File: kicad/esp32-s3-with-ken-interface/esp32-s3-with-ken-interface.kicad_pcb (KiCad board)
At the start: 4 copper layers, 50.8 x 81.3 mm, 28 parts, among them J1 TYPE-C-31-M-12, Q1 UMH3N, U1 CH340C, U2 AMS1117-3.3, U3 XDZ254-2-15-W-2.5-G1, U4 ESP32-S3-WROOM-1, U5 PM254-2-15-W-8.5

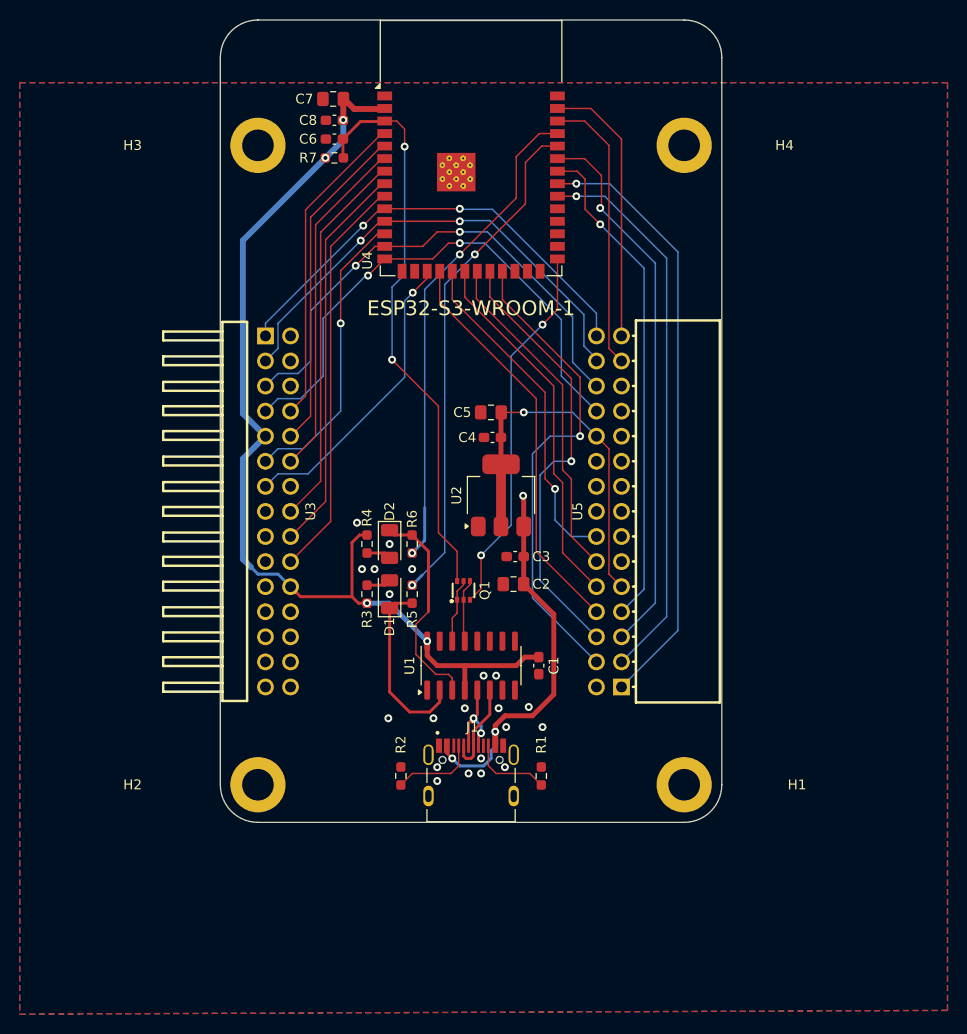
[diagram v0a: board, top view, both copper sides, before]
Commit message: fix left pin header pin assignment
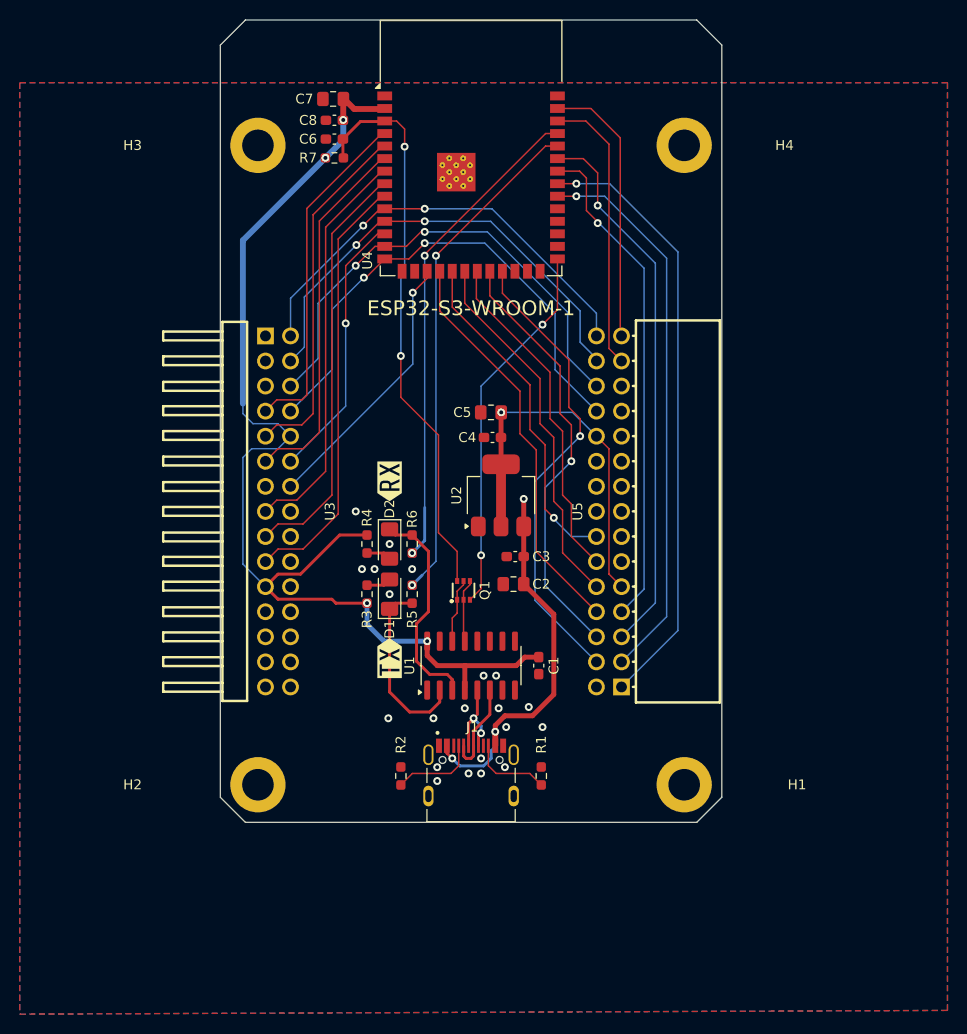
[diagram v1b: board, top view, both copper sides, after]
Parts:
- added kibuzzard-696F5E7C: G***, kibuzzard-696F5E7C, F.Cu at (75.6, 104.0)
- added kibuzzard-696F5E93: G***, kibuzzard-696F5E93, F.Cu at (75.6, 86.1)
- D1, D2: footprint LED_SMD:LED_1206_3216Metric -> LED_SMD:LED_1206_3216Metric_Pad1.42x1.75mm_HandSolder
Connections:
- U3 pad 1: /IO17 -> /ADC_1
- U3 pad 10: /I2S_SCK -> +3V3
- U3 pad 11: /I2C_A_SDA -> /I2S_SD
- U3 pad 12: /I2S_SD -> /I2C_A_SDA
- U3 pad 13: /I2C_A_SCL -> VBUS
- U3 pad 14: VBUS -> /I2C_A_SCL
- U3 pad 15: GND -> /I2S_B_DIN
- U3 pad 16: /I2S_B_DIN -> GND
- U3 pad 17: /IO11 -> /I2S_B_BCLK
- U3 pad 18: /I2S_B_BCLK -> /IO11
- U3 pad 19: /IO13 -> /I2S_B_LRC
- U3 pad 2: /ADC_1 -> /IO17
- U3 pad 20: /I2S_B_LRC -> /IO13
- U3 pad 21: /IO12 -> +3V3
- U3 pad 22: +3V3 -> /IO12
- U3 pad 23: /IO10 -> /I2C_B_SDA
- U3 pad 24: /I2C_B_SDA -> /IO10
- U3 pad 25: /BTN_A -> /I2C_B_SCL
- U3 pad 26: /I2C_B_SCL -> /BTN_A
- U3 pad 27: /BTN_B -> /BTN_C
- U3 pad 28: /BTN_C -> /BTN_B
- U3 pad 29: GND -> /BTN_D
- U3 pad 3: /IO18 -> /ADC_2
- U3 pad 30: /BTN_D -> GND
- U3 pad 4: /ADC_2 -> /IO18
- U3 pad 5: /IO19 -> GND
- U3 pad 6: GND -> /IO19
- U3 pad 7: /IO20 -> /I2S_WS
- U3 pad 8: /I2S_WS -> /IO20
- U3 pad 9: +3V3 -> /I2S_SCK
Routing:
- net +3V3: track 167.6 -> 179.4 mm
- net /I2S_B_BCLK: track 74.9 -> 81.0 mm
- net /I2C_A_SCL: track 64.9 -> 59.6 mm
- net /I2S_B_LRC: track 76.1 -> 81.2 mm
- net /I2S_WS: track 66.8 -> 71.9 mm
- net /I2S_SD: track 69.4 -> 74.4 mm
- net /I2S_SCK: track 68.1 -> 73.2 mm
- net /I2C_A_SDA: track 64.5 -> 59.5 mm
- net /I2S_B_DIN: track 73.2 -> 78.0 mm
- net /BTN_B: track 83.9 -> 79.5 mm
- net /BTN_A: track 79.8 -> 75.6 mm
- net /IO11: track 69.0 -> 65.4 mm
- net /IO10: track 75.6 -> 72.1 mm
- net /IO13: track 69.1 -> 65.5 mm
- net /BTN_C: track 91.0 -> 94.5 mm
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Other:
- outline, holes or cut-outs redrawn

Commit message: adjust traces
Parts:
- moved Q1 0.65 mm to (83.2, 96.5)
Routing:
- net RTS: track 6.57 -> 7.26 mm
- net DTR: track 6.42 -> 7.00 mm
- net RESET: track 57.6 -> 57.0 mm

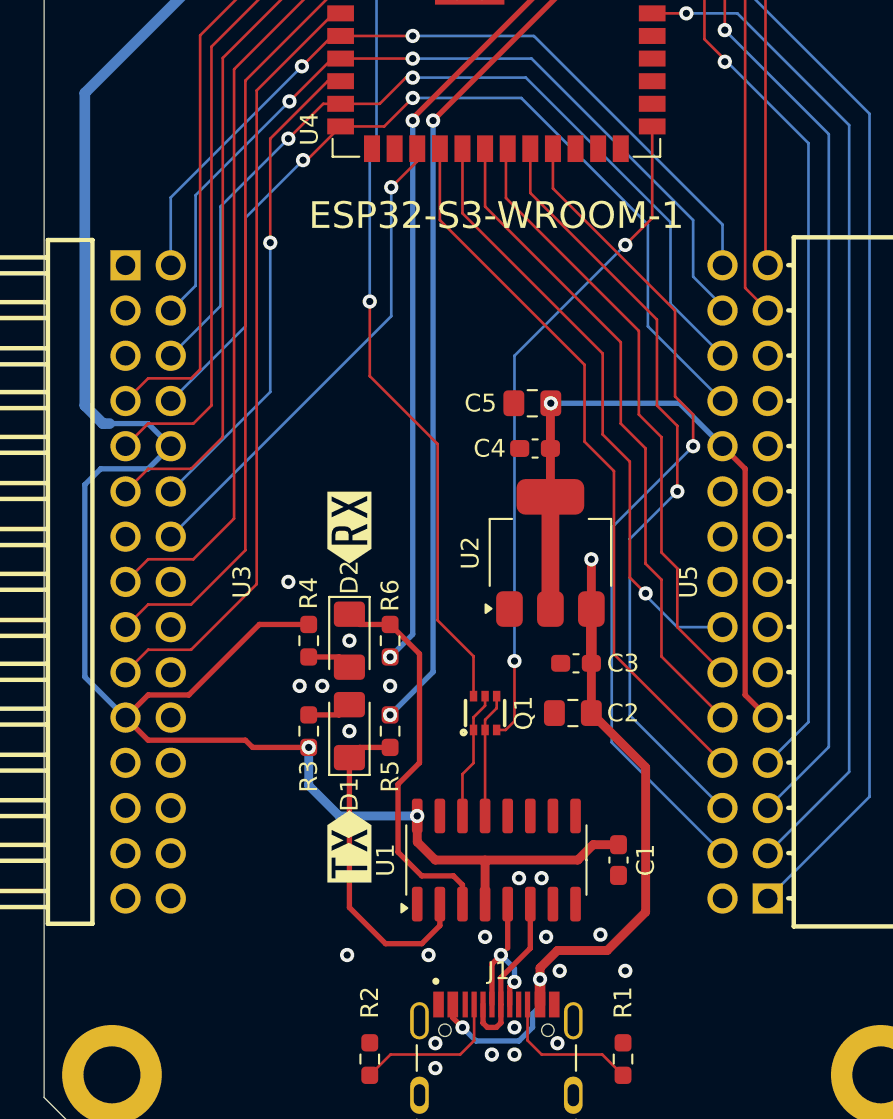
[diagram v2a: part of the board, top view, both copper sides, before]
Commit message: add pin label, adjust routing, add PWM pins
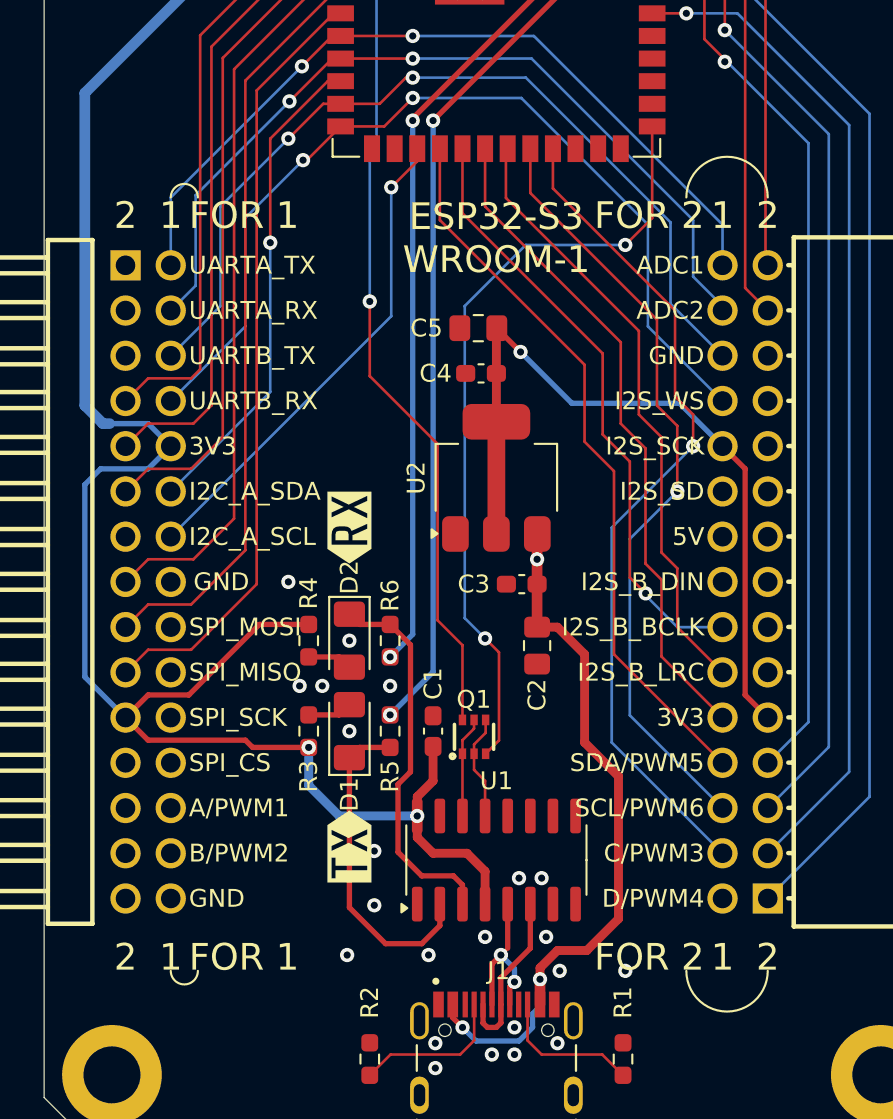
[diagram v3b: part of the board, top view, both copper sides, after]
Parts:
- moved C1 12.7 mm to (80.3, 97.5), turned to 90 degrees
- moved C3 5.39 mm to (85.2, 89.3)
- moved C4 5.19 mm to (83.0, 77.4)
- moved U2 5.19 mm to (83.8, 83.3)
- moved C5 5.19 mm to (82.8, 74.9)
- moved C2 4.29 mm to (86.1, 92.7), turned to -90 degrees
- moved Q1 1.47 mm to (82.6, 97.9)
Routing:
- net GPIO0(D3): track 37.8 -> 44.0 mm
- net VBUS: track 76.6 -> 79.3 mm
- net RTS: track 7.26 -> 5.66 mm
- net RESET: track 57.0 -> 58.1 mm
- net DTR: track 7.00 -> 5.96 mm
- net +3V3: track 179.3 -> 180.0 mm
- net GND: vias 21 -> 22
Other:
- board text added: "1"
- board text added: "2"
- board text added: "3V3"
- board text added: "5V"
- board text added: "A/PWM1"
- board text added: "ADC1"
- board text added: "ADC2"
- board text added: "B/PWM2"
- board text added: "C/PWM3"
- board text added: "D/PWM4"
- board text added: "ESP32-S3 WROOM-1"
- board text added: "FOR 1"
- board text added: "FOR 2"
- board text added: "GND"
- board text added: "I2C_A_SCL"
- board text added: "I2C_A_SDA"
- board text added: "I2S_B_BCLK"
- board text added: "I2S_B_DIN"
- board text added: "I2S_B_LRC"
- board text added: "I2S_SCK"
- board text added: "I2S_SD"
- board text added: "I2S_WS"
- board text added: "SCL/PWM6"
- board text added: "SDA/PWM5"
- board text added: "SPI_CS"
- board text added: "SPI_MISO"
- board text added: "SPI_MOSI"
- board text added: "SPI_SCK"
- board text added: "UARTA_RX"
- board text added: "UARTA_TX"
- board text added: "UARTB_RX"
- board text added: "UARTB_TX"
- board text removed: "ESP32-S3-WROOM-1"

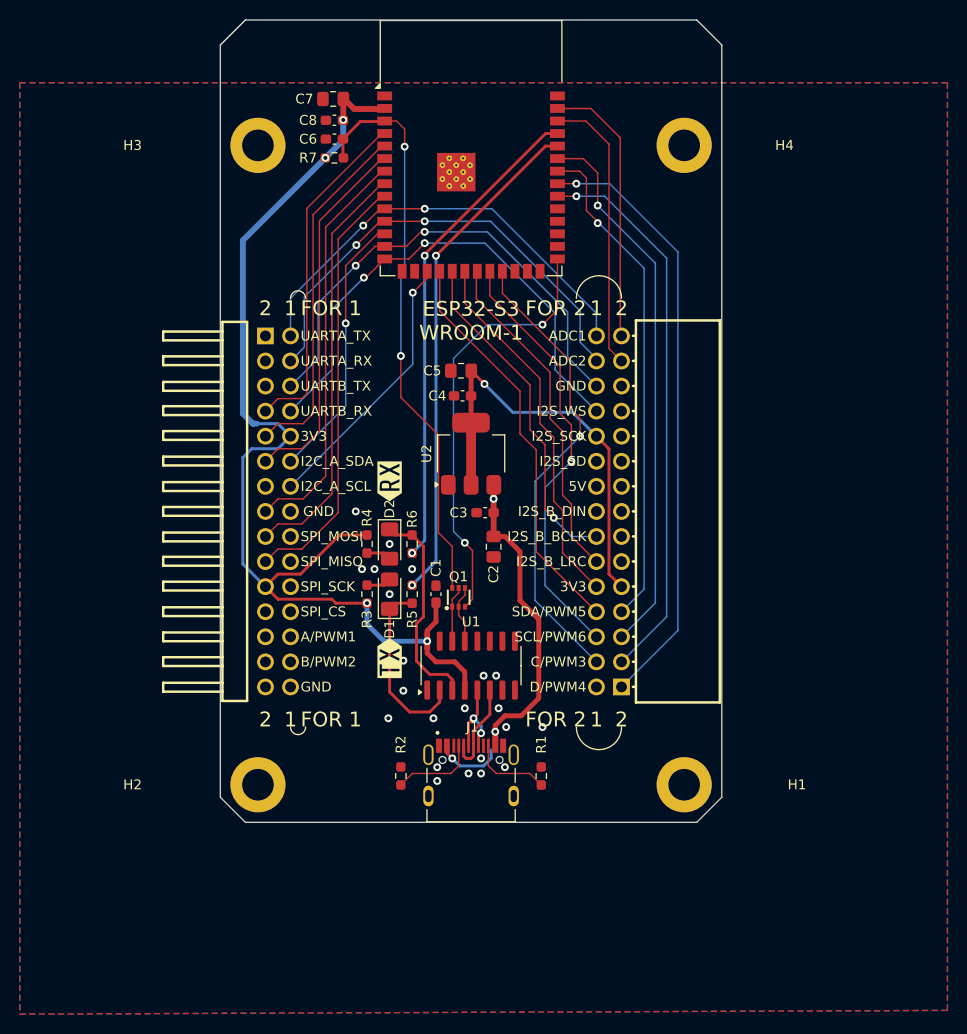
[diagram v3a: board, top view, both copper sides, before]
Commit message: add protect diode, improve trace routing, add vias, add user button and user led, improve schematic, add texts
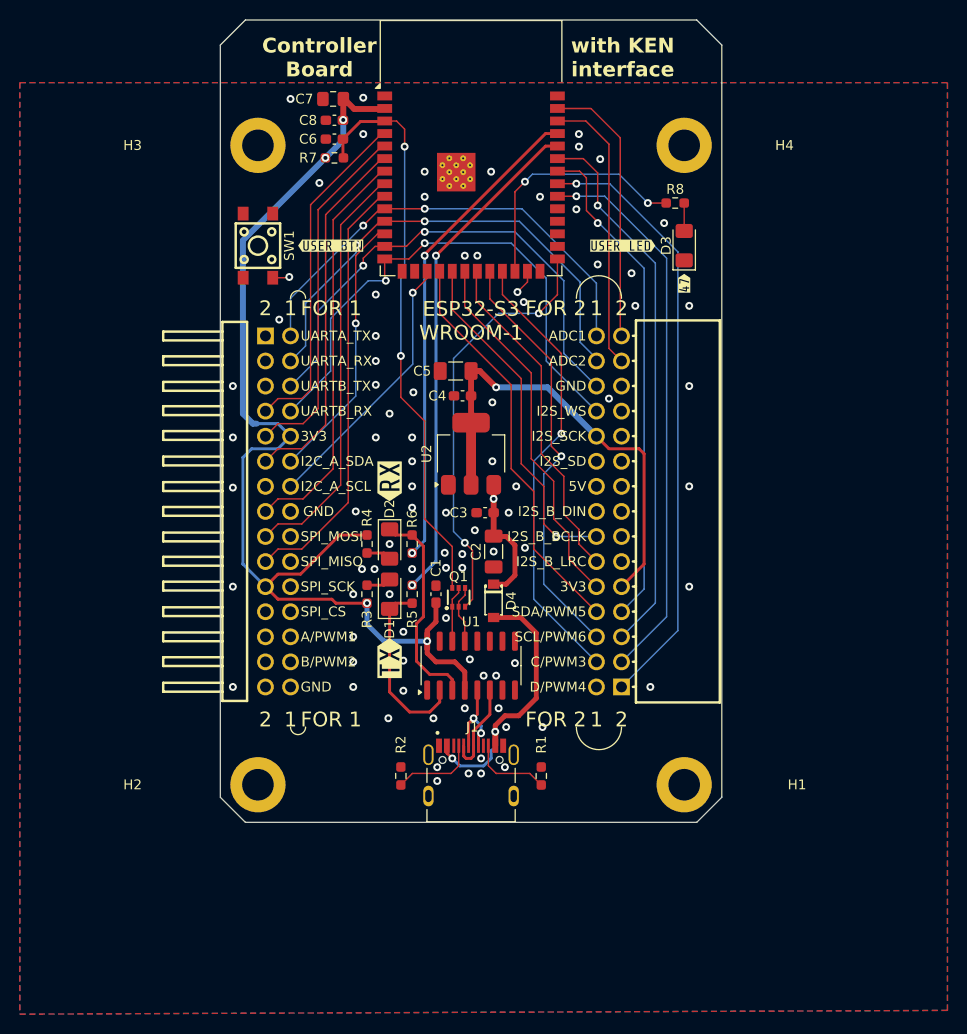
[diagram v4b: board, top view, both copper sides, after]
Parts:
- added D3: LED, LED_SMD:LED_1206_3216Metric_Pad1.42x1.75mm_HandSolder, F.Cu at (105.4, 62.2)
- added D4: B5819W_C109213, B5819W:SOD-123_L2.8-W1.8-LS3.7-RD, F.Cu at (86.1, 98.2)
- added R8: 1k, Resistor_SMD:R_0603_1608Metric_Pad0.98x0.95mm_HandSolder, F.Cu at (104.5, 57.9)
- added SW1: TSC015A03526A, TSC015A03526A:SW-SMD_4P-L4.5-W4.5-P3.00-LS6.8, F.Cu at (62.2, 62.2)
- added kibuzzard-697171B1: G***, kibuzzard-697171B1, F.Cu at (105.4, 66.0)
- added kibuzzard-69717533: G***, kibuzzard-69717533, F.Cu at (69.6, 62.2)
- added kibuzzard-69717543: G***, kibuzzard-69717543, F.Cu at (99.2, 62.2)
- C2, C5: footprint Capacitor_SMD:C_0805_2012Metric_Pad1.18x1.45mm_HandSolder -> Capacitor_SMD:C_1206_3216Metric_Pad1.33x1.80mm_HandSolder
- moved C5 0.55 mm to (82.3, 74.9)
- moved C2 0.49 mm to (86.1, 93.2)
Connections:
- net GPIO0(D3) renamed /ESP32_BOOT
- net RESET renamed /EN
- C2 pad 1: VBUS -> +5V
- C3 pad 1: VBUS -> +5V
- U2 pad 3: VBUS -> +5V
- U3 pad 13: VBUS -> +5V
- U5 pad 17: VBUS -> +5V
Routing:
- net +5V: track 0.00 -> 51.9 mm, vias 0 -> 1
- net VBUS: track 79.3 -> 27.9 mm, vias 3 -> 2
- net /IO48: track 0.00 -> 29.3 mm, vias 0 -> 2
- net /IO47: track 0.00 -> 25.3 mm, vias 0 -> 2
- net +3V3: track 180.0 -> 183.7 mm
- net Net-(D3-A): track 0.00 -> 2.83 mm
- net /IO20: track 52.0 -> 54.6 mm
- net /IO17: track 45.2 -> 47.0 mm
- net /IO18: track 47.7 -> 49.4 mm
- net /IO19: track 49.9 -> 51.5 mm
- net /BTN_B: track 79.5 -> 78.0 mm
- net /IO11: track 65.4 -> 66.3 mm
- net /ESP32_BOOT: track 44.0 -> 43.1 mm
- net /BTN_A: track 75.6 -> 74.9 mm
- net GND: vias 22 -> 84
- added copper zone on In1.Cu, net GND
- added copper zone on In2.Cu, net GND
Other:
- board text added: "Controller Board"
- board text added: "with KEN interface"

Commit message: improve schematic and trace routing, improve silk text, etc
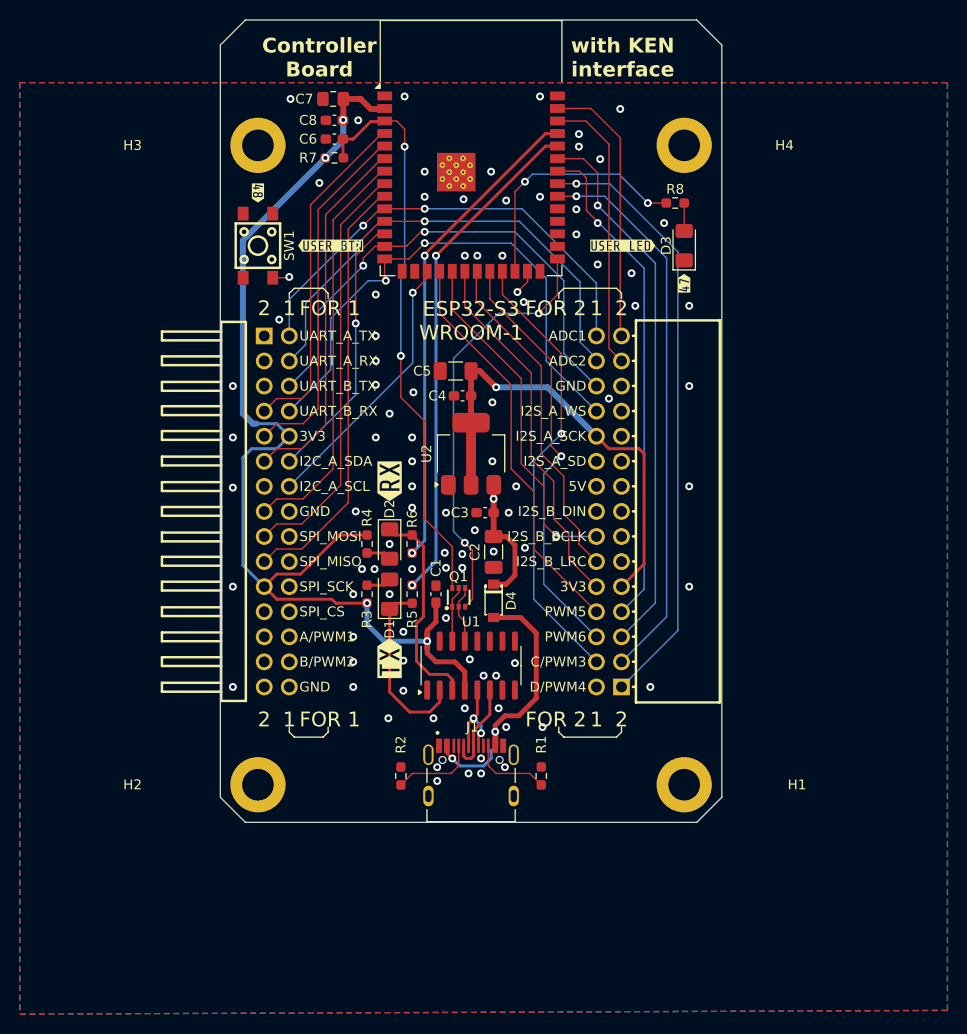
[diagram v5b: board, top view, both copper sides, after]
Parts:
- added kibuzzard-6972B31E: G***, kibuzzard-6972B31E, F.Cu at (62.2, 56.9)
- moved U3 0.13 mm to (64.1, 89.2)
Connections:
- net /ESP32_BOOT renamed /IO0
- net /I2S_SCK renamed /I2S_A_SCK
- net /I2S_SD renamed /I2S_A_SD
- net /I2S_WS renamed /I2S_A_WS
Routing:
- net GND: track 0.07 -> 0.00 mm, vias 84 -> 90
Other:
- board text added: "I2S_A_SCK"
- board text added: "I2S_A_SD"
- board text added: "I2S_A_WS"
- board text added: "PWM5"
- board text added: "PWM6"
- board text added: "UART_A_RX"
- board text added: "UART_A_TX"
- board text added: "UART_B_RX"
- board text added: "UART_B_TX"
- board text added: "version:1.0 date: 20260123"
- board text removed: "I2S_SCK"
- board text removed: "I2S_SD"
- board text removed: "I2S_WS"
- board text removed: "SCL/PWM6"
- board text removed: "SDA/PWM5"
- board text removed: "UARTA_RX"
- board text removed: "UARTA_TX"
- board text removed: "UARTB_RX"
- board text removed: "UARTB_TX"

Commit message: a little update for layouts and routing
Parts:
- moved C2 2.21 mm to (84.5, 91.7), turned to 180 degrees
- moved D4 0.67 mm to (86.1, 97.5)
- moved Q1 0.32 mm to (82.6, 97.5)
- moved C4 0.15 mm to (83.0, 77.6)
- moved C3 0.13 mm to (85.2, 89.2)
- moved C5 0.13 mm to (82.3, 75.1)
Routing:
- net +5V: track 52.0 -> 48.2 mm
- net GND: vias 90 -> 91
